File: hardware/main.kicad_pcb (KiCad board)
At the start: 2 copper layers, 2 parts

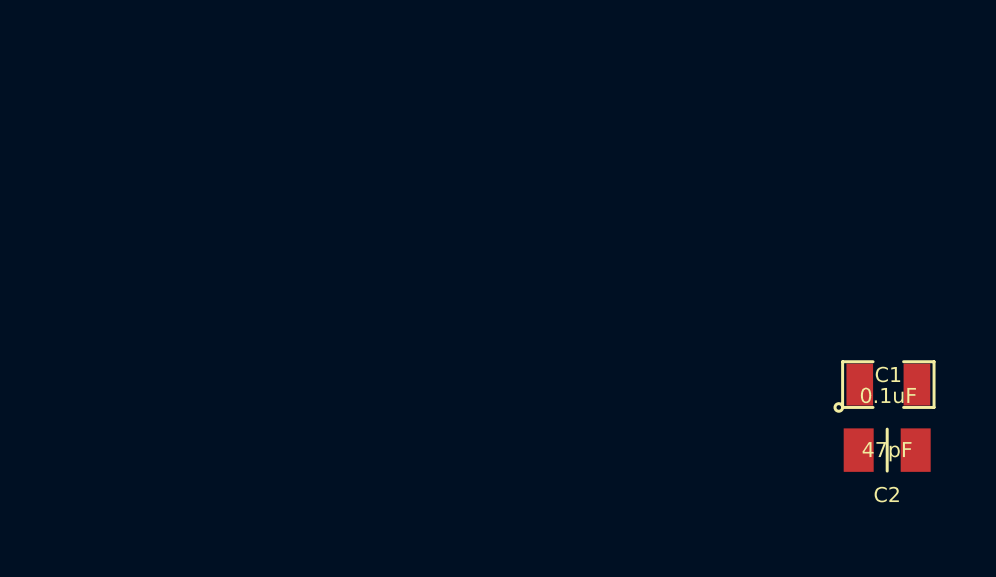
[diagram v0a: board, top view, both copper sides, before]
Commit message: 2-pin header
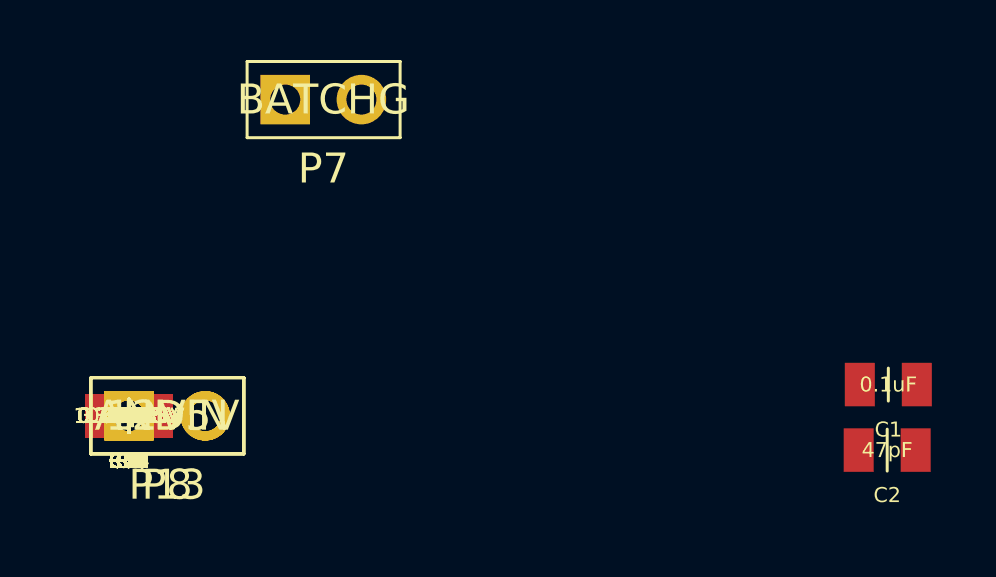
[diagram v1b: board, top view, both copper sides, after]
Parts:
- added C10, C14, C16, C18, C19, C22, C35, C38, C39, C4, C40, C42, C45, C5, C7, C8, C9: 0.1uF, CAPC2012X100N, F.Cu at (123.2, 106.0)
- added C11, C6: 18pF, CAPC2012X100N, F.Cu at (123.2, 106.0)
- added C13, C27, C28, C29, C30, C31, C32, C33, C34: 0.1uF 35V, CAPC2012X100N, F.Cu at (123.2, 106.0)
- added C20: 6.8nF, CAPC2012X100N, F.Cu at (123.2, 106.0)
- added C23, C24: 33nF 35V, CAPC2012X100N, F.Cu at (123.2, 106.0)
- added C25, C26: 100uF 35V, CAPC2012X100N, F.Cu at (123.2, 106.0)
- added C3, C36, C37: 47pF, CAPC2012X100N, F.Cu at (123.2, 106.0)
- added C41, C44: 12pF, CAPC2012X100N, F.Cu at (123.2, 106.0)
- added C43: 4.7uF, CAPC2012X100N, F.Cu at (123.2, 106.0)
- added P13: AND5V, HDRV2W66P254_1X2_508X249X838P, F.Cu at (123.2, 106.0)
- added P7: BATCHG, HDRV2W66P254_1X2_508X249X838P, F.Cu at (128.4, 95.5)
- added P8: 12VIN, HDRV2W66P254_1X2_508X249X838P, F.Cu at (123.2, 106.0)
- added R1, R2, R26, R27, R28, R29, R30, R31, R32, R33, R34, R35, R36, R37, R42, R6, R8: 10K, RESC2012X100N, F.Cu at (123.2, 106.0)
- added R10, R11, R12, R13, R3, R9: 1K, RESC2012X100N, F.Cu at (123.2, 106.0)
- added R14: 0.4, RESC2012X100N, F.Cu at (123.2, 106.0)
- added R15: 760, RESC2012X100N, F.Cu at (123.2, 106.0)
- added R16: 590R, RESC2012X100N, F.Cu at (123.2, 106.0)
- added R17, R18, R19: ???, RESC2012X100N, F.Cu at (123.2, 106.0)
- added R20: 46K, RESC2012X100N, F.Cu at (123.2, 106.0)
- added R21, R43: 100R, RESC2012X100N, F.Cu at (123.2, 106.0)
- added R22: 100k, RESC2012X100N, F.Cu at (123.2, 106.0)
- added R23: 6.8k, RESC2012X100N, F.Cu at (123.2, 106.0)
- added R24: 45.3k, RESC2012X100N, F.Cu at (123.2, 106.0)
- added R25: 10k, RESC2012X100N, F.Cu at (123.2, 106.0)
- added R38, R39: 270R, RESC2012X100N, F.Cu at (123.2, 106.0)
- added R4, R5: 22R, RESC2012X100N, F.Cu at (123.2, 106.0)
- added R40, R41: 27R, RESC2012X100N, F.Cu at (123.2, 106.0)
- added R44: 0R, RESC2012X100N, F.Cu at (123.2, 106.0)
- added R7: 1.5K, RESC2012X100N, F.Cu at (123.2, 106.0)
- C1: footprint SM0805 -> CAPC2012X100N

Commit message: more pcb work
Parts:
- added BT1, BT2: BATTERY, EMPTY, F.Cu at (105.2, 118.9)
- added C12: 100uF 35V, CAPAE660X790N, F.Cu at (111.8, 128.5)
- added C15: 100uF, CAPAE660X790N, F.Cu at (96.9, 105.3)
- added C17: 100uF 15V, CAPAE660X790N, F.Cu at (109.3, 108.1)
- added C21: 100uF, CAPAE660X790N, F.Cu at (94.7, 130.0)
- added D1: DIODE, DIOM5226X220N, F.Cu at (106.3, 140.3)
- added D2: PWR, LEDC3216X100N, F.Cu at (105.2, 118.9)
- added D3: LED, LEDC3216X100N, F.Cu at (104.3, 127.8)
- added M1: Mounting Hole, MTGNP565H328Z565P, F.Cu at (94.9, 119.9)
- added M2: Mounting Hole, MTGNP565H328Z565P, F.Cu at (118.2, 118.2)
- added M3: Mounting Hole, MTGNP565H328Z565P, F.Cu at (112.0, 120.4)
- added M4: Mounting Hole, MTGNP565H328Z565P, F.Cu at (116.8, 138.9)
- added P1: VBAT-TEST, HDRV1W66P254_1X1_254X249X838P, F.Cu at (130.0, 81.3)
- added P11: MOTOR-R, TECONN-2-1445098-2, F.Cu at (44.3, 101.0)
- added P12: MOTOR-L, TECONN-2-1445098-2, F.Cu at (43.1, 120.3)
- added P14: P24, HDRV24W66P254_2X12_3048X503X838P, F.Cu at (125.2, 134.4)
- added P2: USB-VBUS, HDRV1W66P254_1X1_254X249X838P, F.Cu at (130.0, 81.3)
- added P3: SERVO-TILT, HDRV3W66P254_1X3_762X249X838P, F.Cu at (115.1, 76.3)
- added P4: JTAG10, HDRV10W66P254_2X5_1270X503X838P, F.Cu at (141.9, 89.3)
- added P5: POWER-CHARGE, TECONN-2-1445098-2, F.Cu at (59.4, 125.5)
- added P6: POWER, HDRV4W66P254_1X4_1016X249X838P, F.Cu at (135.6, 74.7)
- added P9: BAT, TECONN-2-1445098-3, F.Cu at (67.1, 100.5)

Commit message: qfp48
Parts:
- added Q1: ZXMP2120FFTA, SOT95P237X112_123-3N, F.Cu at (172.6, 119.1)
- added Q2: BD242CG, TO254P1512X997X450-123-3P, F.Cu at (185.3, 98.3)
- added Q3: IRLML2803TRPBF, SOT95P237X112_123-3N, F.Cu at (200.0, 116.6)
- added Q4: IRLML2803TRPBF, SOT95P237X112_123-3N, F.Cu at (190.6, 113.3)
- added S1: BTN_SPST, CKCOMP-PTS525SM10SMTR, F.Cu at (187.8, 125.0)
- added U1: STM32F102C6, QFP50P900X900X160-48N, F.Cu at (184.0, 79.0)

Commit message: more footprints
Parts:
- added U2: BQ24450, SOIC127P1030X265-16N, F.Cu at (63.0, 70.1)
- added U4: AP6502, SOIC127P600X150-9N, F.Cu at (78.7, 55.4)
- added U5: 7408, SOIC127P600X175-14N, F.Cu at (92.3, 56.8)
- added X1: 8MHz, XTAL8045X200N, F.Cu at (77.5, 82.3)
- added X2: 12MHz, XTAL8045X200N, F.Cu at (86.4, 71.9)

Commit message: new packages
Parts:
- added U8: FT312D, QFP80P900X900X160-32N, F.Cu at (172.3, 73.7)
- Q2: footprint TO254P1512X997X450-123-3P -> TO254P1512X997X450-231-3P
- moved U1 11.4 mm to (194.2, 84.1)

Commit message: pqfn
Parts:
- added U3: ZLDO1117, SOT230P700X180-4N, F.Cu at (221.7, 70.1)

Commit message: new pcb
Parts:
- added FB1: MH2029-300Y, INDC2012X110N, F.Cu at (180.0, 143.4)
- added J1: USB_DEBUG, JST_UB-MC5BR3-SD204-4S-NMP, F.Cu at (125.2, 111.3)
- added J2: USB_TO_ANDROID, JST_UB-MC5BR3-SD204-4S-NMP, F.Cu at (138.9, 111.3)
- added L1: 68uH, IND_ASPI-8040S-680M-T, F.Cu at (164.7, 85.3)
- added U6: MC33926, PQFN80P800X800X220-33N, F.Cu at (124.7, 98.6)
- added U7: MC33926, PQFN80P800X800X220-33N, F.Cu at (201.2, 85.3)
- moved U2 139.9 mm to (202.8, 66.9)
- moved P9 122.6 mm to (186.1, 70.9)
- moved U4 116.5 mm to (182.2, 108.8)
- moved P12 111.0 mm to (150.0, 90.6)
- moved BT2 97.4 mm to (199.3, 144.1)
- moved P11 94.4 mm to (138.2, 90.6)
- moved X2 94.0 mm to (172.8, 108.6)
- moved U5 93.3 mm to (175.5, 99.1)
- moved BT1 89.3 mm to (190.8, 144.1)
- moved X1 88.7 mm to (162.2, 108.6)
- moved P1 86.6 mm to (205.5, 123.8)
- moved R4 83.9 mm to (199.9, 140.0)
- moved P3 83.8 mm to (189.1, 115.6)
- moved D3 83.4 mm to (187.6, 123.6)
- moved M3 82.7 mm to (193.9, 108.8)
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
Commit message: layout
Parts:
- C25, C26: footprint CAPC2012X100N -> CAPAE660X790N
- moved U2 174.5 mm to (30.1, 91.4)
- moved R14 160.5 mm to (42.5, 93.5)
- moved C43 153.6 mm to (272.4, 81.7)
- moved C42 153.1 mm to (273.2, 74.9)
- moved M1 151.9 mm to (247.7, 24.6)
- moved U4 151.3 mm to (38.0, 154.6)
- moved R43 150.4 mm to (256.5, 51.2)
- moved R15 149.1 mm to (49.4, 96.6)
- moved R16 144.0 mm to (48.9, 103.0)
- moved C1 143.3 mm to (275.3, 160.1)
- moved R22 142.6 mm to (26.8, 165.7)
- moved L1 142.6 mm to (29.7, 131.3)
- moved J2 140.2 mm to (268.0, 56.5)
- moved R17 139.6 mm to (47.9, 110.7)
- moved U3 137.9 mm to (87.1, 178.6)
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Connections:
- P11 pad 1: N-00000110 -> /Motor Controllers/MOTOR-L-OUT2
- P11 pad 2: N-00000109 (its old number) -> /Motor Controllers/MOTOR-L-OUT1
- P12 pad 1: N-0000089 -> /Motor Controllers/MOTOR-R-OUT2
- P12 pad 2: N-0000081 (its old number) -> /Motor Controllers/MOTOR-R-OUT1
- U6 pad 12: N-00000110 -> /Motor Controllers/MOTOR-L-OUT1
- U6 pad 13: N-00000110 -> /Motor Controllers/MOTOR-L-OUT1
- U6 pad 14: N-00000110 -> /Motor Controllers/MOTOR-L-OUT1
- U6 pad 15: N-00000110 -> /Motor Controllers/MOTOR-L-OUT1
- U6 pad 27: N-00000109 (its old number) -> /Motor Controllers/MOTOR-L-OUT2
- U6 pad 28: N-00000109 (its old number) -> /Motor Controllers/MOTOR-L-OUT2
- U6 pad 29: N-00000109 (its old number) -> /Motor Controllers/MOTOR-L-OUT2
- U6 pad 30: N-00000109 (its old number) -> /Motor Controllers/MOTOR-L-OUT2
- U7 pad 12: N-0000089 -> /Motor Controllers/MOTOR-R-OUT1
- U7 pad 13: N-0000089 -> /Motor Controllers/MOTOR-R-OUT1
- U7 pad 14: N-0000089 -> /Motor Controllers/MOTOR-R-OUT1
- U7 pad 15: N-0000089 -> /Motor Controllers/MOTOR-R-OUT1
- U7 pad 27: N-0000081 (its old number) -> /Motor Controllers/MOTOR-R-OUT2
- U7 pad 28: N-0000081 (its old number) -> /Motor Controllers/MOTOR-R-OUT2
- U7 pad 29: N-0000081 (its old number) -> /Motor Controllers/MOTOR-R-OUT2
- U7 pad 30: N-0000081 (its old number) -> /Motor Controllers/MOTOR-R-OUT2
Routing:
- net +24V: track 0.00 -> 187.6 mm
- net +3.3V: track 0.00 -> 111.6 mm, vias 0 -> 5
- net /Motor Controllers/EN: track 0.00 -> 105.4 mm, vias 0 -> 4
- net /Motor Controllers/MOTOR-R-PWM: track 0.00 -> 62.5 mm, vias 0 -> 2
- net GND: track 0.00 -> 57.4 mm, vias 0 -> 1
- net /Motor Controllers/MOTOR-R-DIR: track 0.00 -> 55.2 mm, vias 0 -> 2
- net /Motor Controllers/MOTOR-L-PWM: track 0.00 -> 52.6 mm
- net /Motor Controllers/MOTOR-L-DIR: track 0.00 -> 39.8 mm
- net N-0000096: track 0.00 -> 24.1 mm, vias 0 -> 4
- net N-0000087: track 0.00 -> 19.4 mm, vias 0 -> 2
- net N-0000097: track 0.00 -> 16.9 mm, vias 0 -> 2
- net /Motor Controllers/MOTOR-L-OUT1: track 0.00 -> 15.5 mm
- net /Motor Controllers/MOTOR-L-OUT2: track 0.00 -> 15.5 mm
- net /Motor Controllers/MOTOR-R-OUT2: track 0.00 -> 15.5 mm
- net /Motor Controllers/MOTOR-R-OUT1: track 0.00 -> 15.4 mm
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- added copper zone on B.Cu, net GND
- added copper zone on F.Cu, net GND
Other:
- net class Default: clearance 0.254 -> 0.2032; trace_width 0.254 -> 0.2032
- rule trace_clearance: 0.254 -> 0.2032
- rule trace_min: 0.254 -> 0.1524
- rule via_min_drill: 0.508 -> 0.3302
- rule via_min_size: 0.889 -> 0.6858
